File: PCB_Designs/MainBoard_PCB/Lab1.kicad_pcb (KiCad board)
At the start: 2 copper layers, 54.5 x 31 mm, 25 parts, among them P1 CONN_01X06, P2 USB_OTG, U1 STM32F411RETx, U2 LM1117_ADJ, Y1 8MHz

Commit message: PCB file created for main board
Nothing really
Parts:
- added C17: 100n, Capacitors_SMD:C_0603_HandSoldering, F.Cu at (254.5, 110.9)
- added C18: 10u, Capacitors_SMD:CP_Elec_10x10.5, F.Cu at (202.1, 123.8)
- added C19: 100n, Capacitors_SMD:C_0603_HandSoldering, F.Cu at (262.0, 106.0)
- added C20: 100n, Capacitors_SMD:C_0603_HandSoldering, F.Cu at (258.2, 140.5)
- added C21: 100n, Capacitors_SMD:C_0603_HandSoldering, F.Cu at (260.1, 133.1)
- added C22: 100n, Capacitors_SMD:C_0603_HandSoldering, F.Cu at (263.8, 120.8)
- added C23: 100n, Capacitors_SMD:C_0603_HandSoldering, F.Cu at (246.8, 122.6)
- added C24: 10u, Capacitors_SMD:CP_Elec_10x10.5, F.Cu at (92.9, 135.9)
- added D1: LED, LEDs:LED_0603, F.Cu at (210.7, 26.0)
- added D2: D, Diodes_SMD:D_0603, F.Cu at (218.2, 24.1)
- added K1: XLR3, Connect:XLR3MC, F.Cu at (189.2, 80.9)
- added L1: FERRITE BEAD 500mA, Resistors_SMD:R_0603, F.Cu at (208.8, 95.9)
- added P3: CONN_02X05, Pin_Headers:Pin_Header_Straight_2x05_Pitch2.54mm, F.Cu at (78.7, 88.3)
- added P4: CONN_01X02, Pin_Headers:Pin_Header_Straight_2x01_Pitch2.54mm, F.Cu at (179.7, 56.5)
- added P5: CONN_02X05, Pin_Headers:Pin_Header_Straight_2x05_Pitch2.54mm, F.Cu at (79.4, 64.8)
- added Q1: BSS138, TO_SOT_Packages_SMD:SOT-23, F.Cu at (156.5, 154.9)
- added Q2: BSS138, TO_SOT_Packages_SMD:SOT-23, F.Cu at (120.9, 130.2)
- added Q3: BSS138, TO_SOT_Packages_SMD:SOT-23, F.Cu at (219.4, 41.0)
- added Q4: BSS138, TO_SOT_Packages_SMD:SOT-23, F.Cu at (251.1, 39.4)
- added Q5: BSS138, TO_SOT_Packages_SMD:SOT-23, F.Cu at (112.0, 41.9)
- added Q6: BSS138, TO_SOT_Packages_SMD:SOT-23, F.Cu at (236.5, 40.0)
- added Q7: BSS138, TO_SOT_Packages_SMD:SOT-23, F.Cu at (230.1, 33.7)
- added R1: 10K, Resistors_SMD:R_0603_HandSoldering, F.Cu at (239.4, 54.0)
- added R11: 330, Resistors_SMD:R_0603_HandSoldering, F.Cu at (253.5, 50.8)
- added R12: 470, Resistors_SMD:R_0603_HandSoldering, F.Cu at (253.5, 65.4)
- added R13: 470, Resistors_SMD:R_0603_HandSoldering, F.Cu at (253.5, 62.2)
- added R14: 470, Resistors_SMD:R_0603_HandSoldering, F.Cu at (248.5, 54.0)
- added R15: 560, Resistors_SMD:R_0603_HandSoldering, F.Cu at (248.5, 58.4)
- added R16: 120, Resistors_SMD:R_0603_HandSoldering, F.Cu at (248.5, 47.6)
- added R17: 560, Resistors_SMD:R_0603_HandSoldering, F.Cu at (244.0, 48.3)
- added R18: 1k, Resistors_SMD:R_0603_HandSoldering, F.Cu at (243.4, 63.5)
- added R19: 10K, Resistors_SMD:R_0603_HandSoldering, F.Cu at (253.5, 54.6)
- added R2: 10K, Resistors_SMD:R_0603_HandSoldering, F.Cu at (238.9, 57.1)
- added R20: 10K, Resistors_SMD:R_0603_HandSoldering, F.Cu at (243.4, 65.4)
- added R21: 10K, Resistors_SMD:R_0603_HandSoldering, F.Cu at (243.4, 55.2)
- added R22: 10K, Resistors_SMD:R_0603_HandSoldering, F.Cu at (248.5, 60.3)
- added R23: 10K, Resistors_SMD:R_0603_HandSoldering, F.Cu at (248.5, 65.4)
- added R24: 10K, Resistors_SMD:R_0603_HandSoldering, F.Cu at (248.5, 62.9)
- added R25: 10K, Resistors_SMD:R_0603_HandSoldering, F.Cu at (238.3, 64.8)
- added R26: 10K, Resistors_SMD:R_0603_HandSoldering, F.Cu at (243.4, 61.0)
- added R3: 10K, Resistors_SMD:R_0603_HandSoldering, F.Cu at (238.3, 61.6)
- added R4: 10K, Resistors_SMD:R_0603_HandSoldering, F.Cu at (238.3, 59.7)
- added R5: 10K, Resistors_SMD:R_0603_HandSoldering, F.Cu at (253.5, 58.4)
- added R6: 10K, Resistors_SMD:R_0603_HandSoldering, F.Cu at (243.4, 50.2)
- added U10: 24C16, Housings_SOIC:SOIC-8_3.9x4.9mm_Pitch1.27mm, F.Cu at (167.5, 46.4)
- added U6: FT232RL, Housings_SSOP:SSOP-28_5.3x10.2mm_Pitch0.65mm, F.Cu at (142.0, 37.0)
- added U7: MAX481CSA, Power_Integrations:SO-8, F.Cu at (198.8, 49.8)
- added U8: LM7805, TO_SOT_Packages_SMD:SOT-223-3Lead_TabPin2, F.Cu at (164.5, 33.7)
- added U9: LM7833, TO_SOT_Packages_SMD:SOT-223-3Lead_TabPin2, F.Cu at (179.7, 34.3)
- C1, C10, C11, C13, C14, C16, C2, C3, C4, C5, C6, C7, C8, C9: footprint Capacitors_SMD:C_0805_HandSoldering -> Capacitors_SMD:C_0603_HandSoldering
- P1: footprint Socket_Strips:Socket_Strip_Straight_1x06 -> Pin_Headers:Pin_Header_Straight_1x06_Pitch2.54mm
- P2: value USB_OTG -> USB_B; footprint Connect:USB_Mini-B -> Connect:USB_B
- R10: value 300 -> 330; footprint Resistors_SMD:R_0805_HandSoldering -> Resistors_SMD:R_0603_HandSoldering
- R7, R8: footprint Resistors_SMD:R_0805_HandSoldering -> Resistors_SMD:R_0603_HandSoldering
- R9: value 200 -> 470; footprint Resistors_SMD:R_0805_HandSoldering -> Resistors_SMD:R_0603_HandSoldering
- U2: value LM1117_ADJ -> TRACO_POWER_DC/DC_CONVERTER; footprint TO_SOT_Packages_SMD:SOT-223 -> Housings_DIP:DIP-24_W7.62mm_Socket
- moved C7 119.5 mm to (252.6, 130.7), turned to 0 degrees
- moved C14 115.7 mm to (256.4, 148.0), turned to 0 degrees
- moved R7 110.7 mm to (248.5, 51.4)
- moved C10 110.5 mm to (235.8, 138.1), turned to 0 degrees
- moved C8 108.3 mm to (245.1, 135.6)
- moved R8 107.2 mm to (252.9, 47.0), turned to 0 degrees
- moved C6 106.5 mm to (250.8, 115.9)
- moved C13 105.5 mm to (243.3, 145.5), turned to 0 degrees
- moved C4 103.2 mm to (241.4, 113.4), turned to 0 degrees
- moved C1 100.5 mm to (232.1, 125.7), turned to 0 degrees
- moved C3 100.0 mm to (233.9, 118.3)
- moved P1 98.1 mm to (124.5, 158.8), turned to 90 degrees
- moved C5 95.9 mm to (239.5, 128.2), turned to 0 degrees
- moved C16 94.7 mm to (248.9, 103.5), turned to 0 degrees
- moved C9 85.2 mm to (237.7, 108.4)
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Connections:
- C11 pad 1: +5V -> +12V
- C12 pad 1: +5V -> +12V
- C13 pad 1: +5V -> +12V
- C14 pad 1: +3V3 -> +5V
- C15 pad 1: +3V3 -> +5V
- P1 pad 6: Net-(P1-Pad6) -> (no net)
- P2 pad 1: +5V -> Net-(L1-Pad1)
- P2 pad 4: Net-(P2-Pad4) -> GND
- R10 pad 1: Net-(R10-Pad1) -> (no net)
- R10 pad 2: GND -> Net-(Q1-Pad3)
- R9 pad 1: +3V3 -> (no net)
- R9 pad 2: Net-(R10-Pad1) -> Net-(Q3-Pad3)
- U1 pad 10: Net-(U1-Pad10) -> (no net)
- U1 pad 11: Net-(U1-Pad11) -> (no net)
- U1 pad 14: Net-(U1-Pad14) -> (no net)
- U1 pad 15: Net-(U1-Pad15) -> (no net)
- U1 pad 16: Net-(U1-Pad16) -> /USB_USART_TX
- U1 pad 17: Net-(U1-Pad17) -> /USB_USART_RX
- U1 pad 2: Net-(U1-Pad2) -> (no net)
- U1 pad 20: Net-(U1-Pad20) -> (no net)
- U1 pad 21: Net-(U1-Pad21) -> (no net)
- U1 pad 22: Net-(U1-Pad22) -> (no net)
- U1 pad 23: Net-(U1-Pad23) -> (no net)
- U1 pad 24: Net-(U1-Pad24) -> (no net)
- U1 pad 25: Net-(U1-Pad25) -> (no net)
- U1 pad 26: Net-(U1-Pad26) -> (no net)
- U1 pad 27: Net-(U1-Pad27) -> (no net)
- U1 pad 28: Net-(U1-Pad28) -> (no net)
- U1 pad 29: Net-(U1-Pad29) -> /LCD_I2C_SCL
- U1 pad 3: Net-(U1-Pad3) -> (no net)
- U1 pad 33: Net-(U1-Pad33) -> (no net)
- U1 pad 34: Net-(U1-Pad34) -> (no net)
- U1 pad 35: Net-(U1-Pad35) -> (no net)
- U1 pad 36: Net-(U1-Pad36) -> (no net)
- U1 pad 37: Net-(U1-Pad37) -> /LCD_BACKLIGHT
- U1 pad 38: Net-(U1-Pad38) -> /INT_BUTTA
- U1 pad 39: Net-(U1-Pad39) -> /INT_BUTTB
- U1 pad 4: Net-(U1-Pad4) -> (no net)
- U1 pad 40: Net-(U1-Pad40) -> /BUTT_I2C_SDA
- U1 pad 41: Net-(U1-Pad41) -> /BUTT_I2C_SCL
- U1 pad 42: Net-(U1-Pad42) -> /USART1_TX
- U1 pad 43: Net-(U1-Pad43) -> /USART1_RX
- U1 pad 44: Net-(U1-Pad44) -> /RX485_RE_DE
- U1 pad 45: Net-(U1-Pad45) -> (no net)
- U1 pad 50: Net-(U1-Pad50) -> (no net)
- U1 pad 51: Net-(U1-Pad51) -> (no net)
- U1 pad 52: Net-(U1-Pad52) -> (no net)
- U1 pad 53: Net-(U1-Pad53) -> (no net)
- U1 pad 54: Net-(U1-Pad54) -> (no net)
- U1 pad 55: Net-(U1-Pad55) -> /LCD_I2C_SDA
- U1 pad 56: Net-(U1-Pad56) -> (no net)
- U1 pad 57: Net-(U1-Pad57) -> (no net)
- U1 pad 58: Net-(U1-Pad58) -> /INT_ROTARY
- U1 pad 59: Net-(U1-Pad59) -> (no net)
- U1 pad 8: Net-(U1-Pad8) -> (no net)
- U1 pad 9: Net-(U1-Pad9) -> (no net)
- U2 pad 1: Net-(R10-Pad1) -> GND
- U2 pad 2: +3V3 -> +5V
- U2 pad 3: +5V -> /GNDEXT
- U2 pad 4: +3V3 -> /VDD5EXT
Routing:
- net +3V3: track 127.8 -> 0.00 mm
- net GND: track 55.7 -> 0.00 mm, vias 3 -> 0
- net +5V: track 24.0 -> 0.00 mm
- net /NRST: track 22.6 -> 0.00 mm, vias 2 -> 0
- net /SWDIO: track 18.0 -> 0.00 mm, vias 2 -> 0
- net Net-(C2-Pad1): track 16.1 -> 0.00 mm
- net Net-(C3-Pad1): track 16.0 -> 0.00 mm
- net Net-(R10-Pad1): track 13.6 -> 0.00 mm
- net /SWCLK: track 11.0 -> 0.00 mm
- net Net-(C5-Pad2): track 2.91 -> 0.00 mm
- net Net-(R8-Pad1): track 2.33 -> 0.00 mm
- removed copper zone on B.Cu, net GND
- removed copper zone on F.Cu, net GND
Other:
- board outline removed
- net class Default: via_dia 0.35 -> 0.6; via_drill 0.3 -> 0.4
- rule pad_to_mask_clearance: 0.2 -> 0
- rule trace_min: 0.15 -> 0.2
- rule via_min_size: 0.35 -> 0.4

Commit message: Main PCB work in progress...
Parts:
- added U3: 6N137, Housings_DIP:DIP-8_W7.62mm, F.Cu at (147.8, 87.4)
- added U4: 6N137, Housings_DIP:DIP-8_W7.62mm, F.Cu at (147.8, 62.5)
- added U5: 6N137, Housings_DIP:DIP-8_W7.62mm, F.Cu at (147.8, 74.7)
- C12, C15, C18, C24: footprint Capacitors_SMD:CP_Elec_10x10.5 -> Capacitors_Tantalum_SMD:CP_Tantalum_Case-C_EIA-6032-28_Hand
- C13: value 100nC -> 100n
- U2: value TRACO_POWER_DC/DC_CONVERTER -> DC/DC_CONV; footprint Housings_DIP:DIP-24_W7.62mm_Socket -> Converters_DCDC_ACDC:DCDC-Conv_TRACO_TED-xxxx_Single
- U8: value LM7805 -> LT1129CST-5
- U9: value LM7833 -> LT1129CST-3.3
- moved C19 176.6 mm to (88.2, 74.4), turned to 180 degrees
- moved C17 169.7 mm to (88.4, 76.4), turned to 180 degrees
- moved C13 162.8 mm to (87.4, 98.6), turned to 90 degrees
- moved R18 162.6 mm to (85.5, 102.4), turned to 90 degrees
- moved C14 159.7 mm to (102.4, 105.7), turned to 90 degrees
- moved D2 156.6 mm to (82.3, 101.9), turned to 270 degrees
- moved C11 151.4 mm to (85.5, 98.6), turned to 90 degrees
- moved C23 147.2 mm to (102.4, 94.2), turned to 90 degrees
- moved Q4 146.5 mm to (115.6, 95.0), turned to 270 degrees
- moved D1 144.8 mm to (87.6, 102.4), turned to 90 degrees
- moved R19 142.8 mm to (115.6, 91.4)
- moved R24 142.8 mm to (110.1, 98.0)
- moved C6 142.1 mm to (114.9, 74.3)
- moved C8 141.5 mm to (114.9, 80.3)
- moved C16 137.8 mm to (117.1, 63.2), turned to 180 degrees
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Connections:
- C20 pad 1: /GNDEXT -> /VDD5EXT
- C20 pad 2: /VDD5EXT -> /GNDEXT
- C21 pad 1: /GNDEXT -> /VDD5EXT
- C21 pad 2: /VDD5EXT -> /GNDEXT
- C22 pad 1: /GNDEXT -> /VDD5EXT
- C22 pad 2: /VDD5EXT -> /GNDEXT
- P1 pad 6: (no net) -> Net-(P1-Pad6)
- P3 pad 10: (no net) -> Net-(P3-Pad10)
- P3 pad 4: (no net) -> Net-(P3-Pad4)
- P3 pad 6: (no net) -> Net-(P3-Pad6)
- P3 pad 8: (no net) -> Net-(P3-Pad8)
- P5 pad 10: (no net) -> Net-(P5-Pad10)
- P5 pad 4: (no net) -> Net-(P5-Pad4)
- P5 pad 6: (no net) -> Net-(P5-Pad6)
- P5 pad 8: (no net) -> Net-(P5-Pad8)
- R10 pad 1: (no net) -> Net-(R10-Pad1)
- R11 pad 1: (no net) -> Net-(R11-Pad1)
- R14 pad 2: (no net) -> Net-(R14-Pad2)
- R9 pad 1: (no net) -> Net-(R9-Pad1)
- U1 pad 10: (no net) -> Net-(U1-Pad10)
- U1 pad 11: (no net) -> Net-(U1-Pad11)
- U1 pad 14: (no net) -> Net-(U1-Pad14)
- U1 pad 15: (no net) -> Net-(U1-Pad15)
- U1 pad 2: (no net) -> Net-(U1-Pad2)
- U1 pad 20: (no net) -> Net-(U1-Pad20)
- U1 pad 21: (no net) -> Net-(U1-Pad21)
- U1 pad 22: (no net) -> Net-(U1-Pad22)
- U1 pad 23: (no net) -> Net-(U1-Pad23)
- U1 pad 24: (no net) -> Net-(U1-Pad24)
- U1 pad 25: (no net) -> Net-(U1-Pad25)
- U1 pad 26: (no net) -> Net-(U1-Pad26)
- U1 pad 27: (no net) -> Net-(U1-Pad27)
- U1 pad 28: (no net) -> Net-(U1-Pad28)
- U1 pad 3: (no net) -> Net-(U1-Pad3)
- U1 pad 33: (no net) -> Net-(U1-Pad33)
- U1 pad 34: (no net) -> Net-(U1-Pad34)
- U1 pad 35: (no net) -> Net-(U1-Pad35)
- U1 pad 36: (no net) -> Net-(U1-Pad36)
- U1 pad 4: (no net) -> Net-(U1-Pad4)
- U1 pad 45: (no net) -> Net-(U1-Pad45)
- U1 pad 50: (no net) -> Net-(U1-Pad50)
- U1 pad 51: (no net) -> Net-(U1-Pad51)
- U1 pad 52: (no net) -> Net-(U1-Pad52)
- U1 pad 53: (no net) -> Net-(U1-Pad53)
- U1 pad 54: (no net) -> Net-(U1-Pad54)
- U1 pad 56: (no net) -> Net-(U1-Pad56)
- U1 pad 57: (no net) -> Net-(U1-Pad57)
- U1 pad 59: (no net) -> Net-(U1-Pad59)
- U1 pad 8: (no net) -> Net-(U1-Pad8)
- U1 pad 9: (no net) -> Net-(U1-Pad9)
- U10 pad 1: (no net) -> Net-(U10-Pad1)
- U2 pad 1: GND -> +5V
- U2 pad 10: (no net) -> /GNDEXT
- U2 pad 11: (no net) -> /VDD5EXT
- U2 pad 12: (no net) -> GND
- U2 pad 13: (no net) -> GND
- U2 pad 14: (no net) -> /VDD5EXT
- U2 pad 15: (no net) -> /GNDEXT
- U2 pad 2: +5V -> Net-(U2-Pad2)
- U2 pad 22: (no net) -> Net-(U2-Pad22)
- U2 pad 23: (no net) -> Net-(U2-Pad23)
- U2 pad 24: (no net) -> +5V
- U2 pad 3: /GNDEXT -> Net-(U2-Pad3)
- U6 pad 10: (no net) -> Net-(U6-Pad10)
- U6 pad 11: (no net) -> Net-(U6-Pad11)
- U6 pad 12: (no net) -> Net-(U6-Pad12)
- U6 pad 13: (no net) -> Net-(U6-Pad13)
- U6 pad 14: (no net) -> Net-(U6-Pad14)
- U6 pad 17: (no net) -> Net-(U6-Pad17)
- U6 pad 19: (no net) -> Net-(U6-Pad19)
- U6 pad 2: (no net) -> Net-(U6-Pad2)
- U6 pad 22: (no net) -> Net-(U6-Pad22)
- U6 pad 23: (no net) -> Net-(U6-Pad23)
- U6 pad 27: (no net) -> Net-(U6-Pad27)
- U6 pad 28: (no net) -> Net-(U6-Pad28)
- U6 pad 3: (no net) -> Net-(U6-Pad3)
- U6 pad 4: (no net) -> Net-(U6-Pad4)
- U6 pad 6: (no net) -> Net-(U6-Pad6)
- U6 pad 9: (no net) -> Net-(U6-Pad9)
- U8 pad 1: (no net) -> +12V
- U8 pad 2: (no net) -> GND
- U8 pad 3: (no net) -> +5V
- U9 pad 1: (no net) -> +12V
- U9 pad 2: (no net) -> GND
- U9 pad 3: (no net) -> +3V3
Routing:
- net +3V3: track 0.00 -> 101.3 mm
- net +5V: track 0.00 -> 82.5 mm
- net /VDD5EXT: track 0.00 -> 51.2 mm
- net GND: track 0.00 -> 49.9 mm
- net /INT_BUTTB: track 0.00 -> 36.9 mm
- net /GNDEXT: track 0.00 -> 31.8 mm
- net /BUTT_I2C_SDA: track 0.00 -> 30.1 mm
- net /BUTT_I2C_SCL: track 0.00 -> 28.7 mm, vias 0 -> 1
- net /INT_ROTARY: track 0.00 -> 27.7 mm
- net /INT_BUTTA: track 0.00 -> 25.6 mm
- net +12V: track 0.00 -> 23.2 mm
- net Net-(R14-Pad1): track 0.00 -> 22.7 mm
- net /USB_USART_RX: track 0.00 -> 22.7 mm, vias 0 -> 2
- net Net-(K1-Pad3): track 0.00 -> 19.6 mm
- net Net-(K1-Pad2): track 0.00 -> 19.6 mm
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- added copper zone on F.Cu, net GND

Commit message: First PCB version of main board
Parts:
- added P6: CONN_02X05, Pin_Headers:Pin_Header_Straight_2x05_Pitch2.54mm, F.Cu at (109.0, 83.4)
- K1: footprint Connect:XLR3MC -> Pin_Headers:Pin_Header_Straight_1x03_Pitch1.27mm
- U3, U4, U5: footprint Housings_DIP:DIP-8_W7.62mm -> Housings_DIP:DIP-8_W7.62mm_LongPads
- U8, U9: footprint TO_SOT_Packages_SMD:SOT-223-3Lead_TabPin2 -> TO_SOT_Packages_SMD:SOT-223
- moved K1 51.8 mm to (132.6, 89.9), turned to 0 degrees
- moved R15 43.9 mm to (126.1, 96.1)
- moved R16 43.9 mm to (126.1, 91.6)
- moved R17 43.9 mm to (126.1, 87.0)
- moved U7 42.4 mm to (120.9, 91.4)
- moved U2 41.9 mm to (146.8, 81.5)
- moved C22 39.8 mm to (129.9, 48.0)
- moved C20 39.8 mm to (134.0, 48.0)
- moved C21 39.8 mm to (132.0, 48.0)
- moved C5 36.6 mm to (92.5, 73.3)
- moved C1 36.0 mm to (94.4, 73.3)
- moved C9 35.5 mm to (87.9, 73.4)
- moved C12 35.4 mm to (49.7, 81.1)
- moved Q1 35.4 mm to (105.3, 60.6)
- moved R1 35.4 mm to (102.0, 60.7)
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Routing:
- net +5V: track 82.5 -> 184.2 mm, vias 0 -> 3
- net +3V3: track 101.3 -> 188.6 mm, vias 0 -> 6
- net /GNDEXT: track 31.8 -> 112.9 mm
- net Net-(R12-Pad1): track 5.44 -> 82.0 mm, vias 0 -> 1
- net /VDD5EXT: track 51.2 -> 117.9 mm
- net Net-(Q3-Pad3): track 6.10 -> 54.0 mm
- net GND: track 49.9 -> 89.6 mm, vias 0 -> 5
- net Net-(P6-Pad7): track 0.00 -> 30.4 mm, vias 0 -> 1
- net /LCD_I2C_SDA: track 2.24 -> 30.4 mm, vias 0 -> 2
- net Net-(P6-Pad2): track 0.00 -> 24.7 mm, vias 0 -> 1
- net Net-(P6-Pad9): track 0.00 -> 24.6 mm, vias 0 -> 1
- net Net-(P6-Pad5): track 0.00 -> 24.0 mm, vias 0 -> 1
- net /NRST: track 2.27 -> 25.2 mm, vias 0 -> 1
- net /SWDIO: track 0.00 -> 22.0 mm, vias 0 -> 1
- net /SWCLK: track 0.00 -> 19.5 mm, vias 0 -> 2
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- added copper zone on B.Cu, net GND
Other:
- board outline added: 113.5 x 55.6 mm

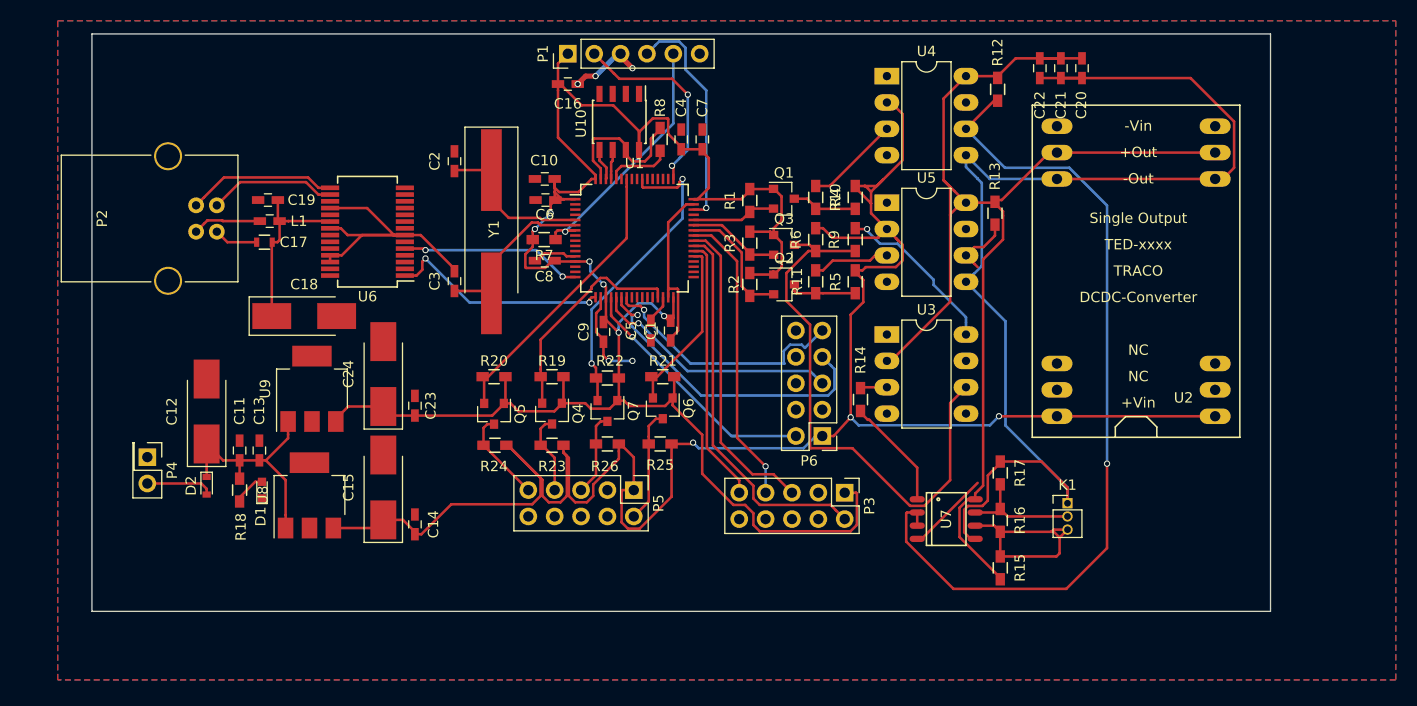
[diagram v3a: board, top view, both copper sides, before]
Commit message: Added 3.3v to FT232RL, use larger power tracks
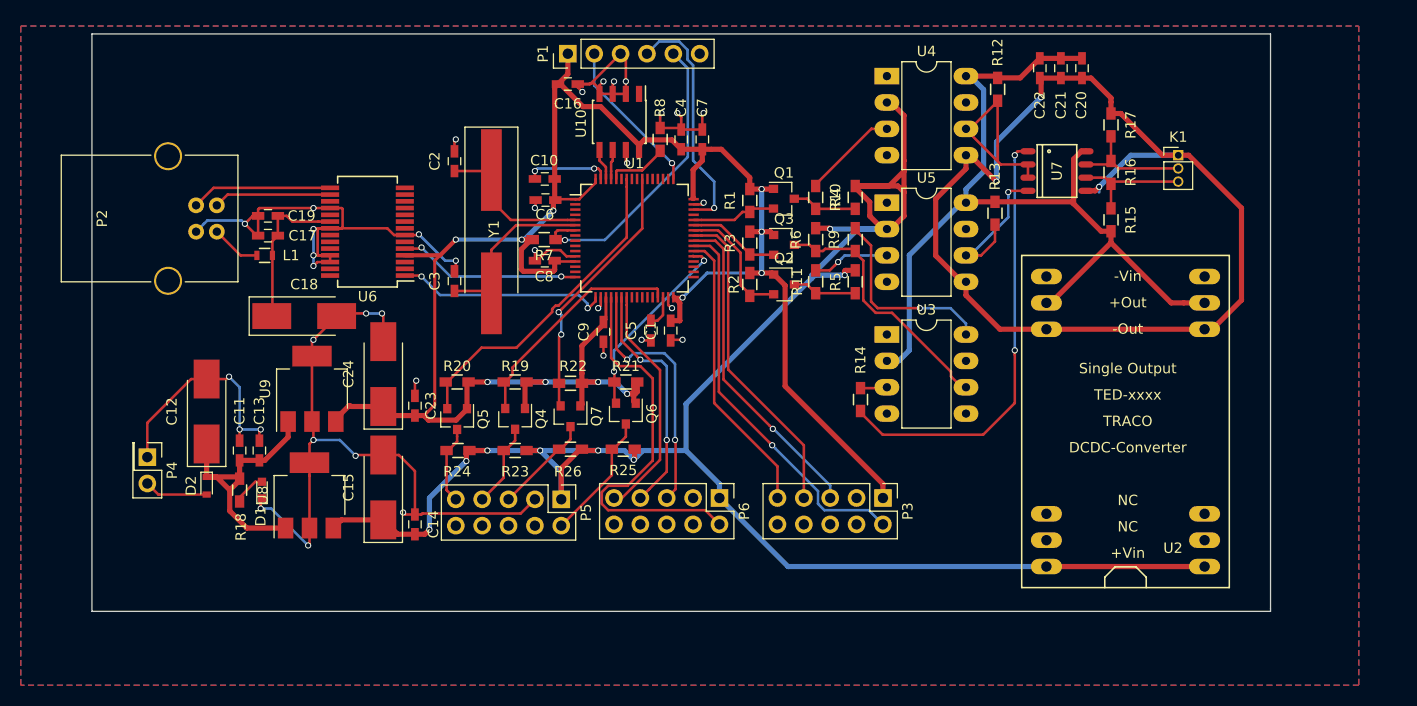
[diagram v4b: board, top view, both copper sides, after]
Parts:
- U8: value LT1129CST-5 -> UA78M05IDCY
- U9: value LT1129CST-3.3 -> UA78M33CDCY
- moved R17 35.2 mm to (136.8, 53.5)
- moved K1 35.2 mm to (143.3, 56.4)
- moved R15 35.2 mm to (136.8, 62.6)
- moved U7 35.2 mm to (131.6, 57.9)
- moved R16 35.2 mm to (136.8, 58.0)
- moved U2 14.5 mm to (145.8, 96.0)
- moved P6 11.6 mm to (99.1, 89.4), turned to 270 degrees
- moved P5 7.04 mm to (83.8, 89.5)
- moved P3 3.72 mm to (114.8, 89.4)
- moved R24 3.59 mm to (73.9, 84.8)
- moved Q7 3.59 mm to (84.7, 81.5)
- moved R25 3.59 mm to (89.8, 84.7)
- moved R26 3.59 mm to (84.7, 84.7)
- moved Q4 3.59 mm to (79.4, 81.8)
- moved Q5 3.59 mm to (73.8, 81.8)
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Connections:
- U6 pad 4: Net-(U6-Pad4) -> +3V3
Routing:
- net GND: track 89.6 -> 193.7 mm, vias 5 -> 38
- net Net-(R12-Pad1): track 82.0 -> 19.7 mm, vias 1 -> 0
- net Net-(R14-Pad1): track 11.3 -> 42.5 mm, vias 0 -> 2
- net Net-(Q3-Pad3): track 54.0 -> 25.1 mm
- net /VDD5EXT: track 117.9 -> 90.5 mm
- net Net-(P6-Pad2): track 24.7 -> 38.0 mm, vias 1 -> 0
- net +3V3: track 188.6 -> 201.5 mm, vias 6 -> 11
- net Net-(K1-Pad3): track 21.1 -> 11.6 mm
- net Net-(P6-Pad7): track 30.4 -> 23.3 mm, vias 1 -> 2
- net /GNDEXT: track 112.9 -> 106.8 mm, vias 0 -> 3
- net /LCD_I2C_SDA: track 30.4 -> 25.4 mm
- net +12V: track 23.2 -> 27.6 mm
- net /SWCLK: track 19.5 -> 15.2 mm, vias 2 -> 1
- net /NRST: track 25.2 -> 29.3 mm
- net /INT_ROTARY: track 27.7 -> 31.7 mm
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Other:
- net class Power added: clearance 0.2, trace_width 0.3, via_dia 0.6, via_drill 0.4
